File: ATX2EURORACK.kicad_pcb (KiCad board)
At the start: 2 copper layers, 58.4 x 33 mm, 7 parts, among them J1 ATX-20, J2 PWR_ON_OK, J3 Conn_02x08_Odd_Even

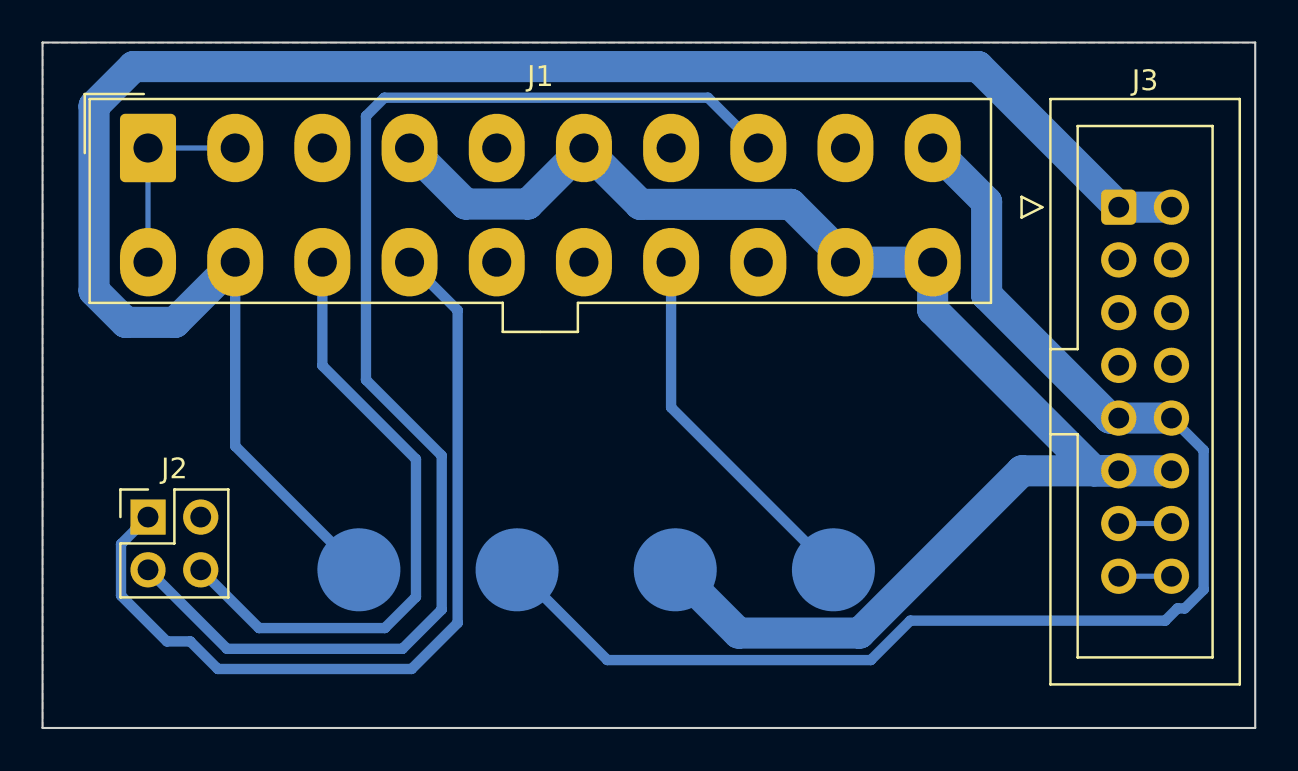
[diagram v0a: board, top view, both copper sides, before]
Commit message: Rounded the tracks
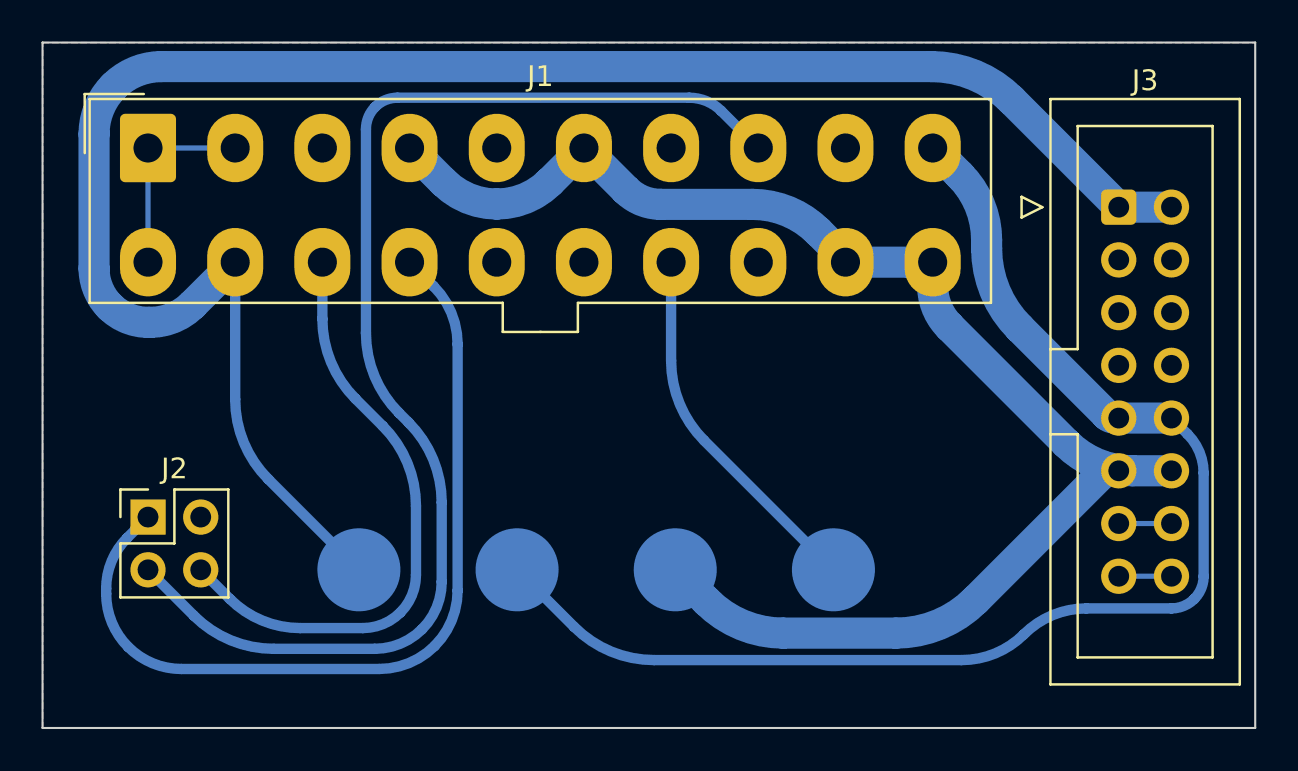
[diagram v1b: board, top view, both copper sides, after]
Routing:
- net +5V: track 72.7 -> 70.5 mm
- net +12V: track 64.7 -> 63.3 mm
- net /POWER_OK: track 62.1 -> 60.7 mm
- net GND: track 48.2 -> 46.9 mm
- net -12V: track 90.3 -> 89.1 mm
- net /POWER_ON: track 41.9 -> 42.7 mm

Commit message: Updates
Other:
- board text added: "ATX2EURORACK"
- board text added: "ON/OFF"
- board text added: "STATUS"
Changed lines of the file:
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@@
     (pad_to_mask_clearance 0)
     (pcbplotparams
-      (layerselection 0x00010fc_ffffffff)
+      (layerselection 0x0001000_fffffffe)
       (disableapertmacros false)
       (usegerberextensions false)
@@
       (hpglpendiameter 15.000000)
       (dxfpolygonmode true)
-      (dxfimperialunits true)
+      (dxfimperialunits false)
       (dxfusepcbnewfont true)
       (psnegative false)
@@
       (sketchpadsonfab false)
       (subtractmaskfromsilk false)
-      (outputformat 1)
+      (outputformat 3)
       (mirror false)
-      (drillshape 1)
+      (drillshape 2)
       (scaleselection 1)
       (outputdirectory "")
@@
     (fp_line (start 31.05 2.3) (end 31.05 -1) (layer "F.Fab") (width 0.1))
     (fp_line (start 40.5 -2.25) (end -2.7 -2.25) (layer "F.Fab") (width 0.1))
-    (pad "1" thru_hole roundrect (at 0 0) (size 2.7 3.3) (drill 1.4) (layers *.Cu *.Mask) (roundrect_rratio 0.092593)
+    (pad "1" thru_hole roundrect (at 0 0) (size 2.7 3.3) (drill 1.4) (layers *.Cu *.Mask) (roundrect_rratio 0.09259296296)
       (net 1 "Net-(J1-Pad1)") (pinfunction "+3.3V") (pintype "power_out"))
     (pad "2" thru_hole oval (at 4.2 0) (size 2.7 3.3) (drill 1.4) (layers *.Cu *.Mask)
@@
     (fp_line (start -3.18 6.84) (end -1.98 6.84) (layer "F.Fab") (width 0.1))
     (fp_line (start 5.72 22.88) (end -3.18 22.88) (layer "F.Fab") (width 0.1))
-    (pad "1" thru_hole roundrect (at 0 0) (size 1.7 1.7) (drill 1) (layers *.Cu *.Mask) (roundrect_rratio 0.147059)
+    (pad "1" thru_hole roundrect (at 0 0) (size 1.7 1.7) (drill 1) (layers *.Cu *.Mask) (roundrect_rratio 0.1470588235)
       (net 7 "-12V") (pinfunction "Pin_1") (pintype "passive"))
     (pad "2" thru_hole circle (at 2.54 0) (size 1.7 1.7) (drill 1) (layers *.Cu *.Mask)
@@
   (gr_line (start 116.84 81.28) (end 175.26 81.28) (layer "Edge.Cuts") (width 0.1))
   (gr_line (start 175.26 81.28) (end 175.26 114.3) (layer "Edge.Cuts") (width 0.1))
+  (gr_text "ATX2EURORACK" (at 144.927075 103.014708) (layer "F.SilkS")
+    (effects (font (size 2 2) (thickness 0.15)))
+  )
+  (gr_text "ON/OFF" (at 123.441921 101.370148) (layer "F.SilkS")
+    (effects (font (size 1.5 1.5) (thickness 0.3)))
+  )
+  (gr_text "STATUS" (at 122.937748 109.315241) (layer "F.SilkS")
+    (effects (font (size 1.5 1.5) (thickness 0.3)))
+  )
   (segment (start 121.92 86.36) (end 121.92 91.86) (width 0.25) (layer "B.Cu") (net 1))
   (segment (start 121.92 86.36) (end 126.12 86.36) (width 0.25) (layer "B.Cu") (net 1))
